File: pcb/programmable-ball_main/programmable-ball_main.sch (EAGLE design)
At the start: 19 parts, among them J1 12402012E212A, P1 S2B-ZR-SM4A-TF, Q1 DMG2305UX-13, SW1 CAS-120CAS-120B1, U1 MDBT50Q-1MV2, U2 AP2112K-3.3TRG1, Y1 FC-135_32.7680KA-A0

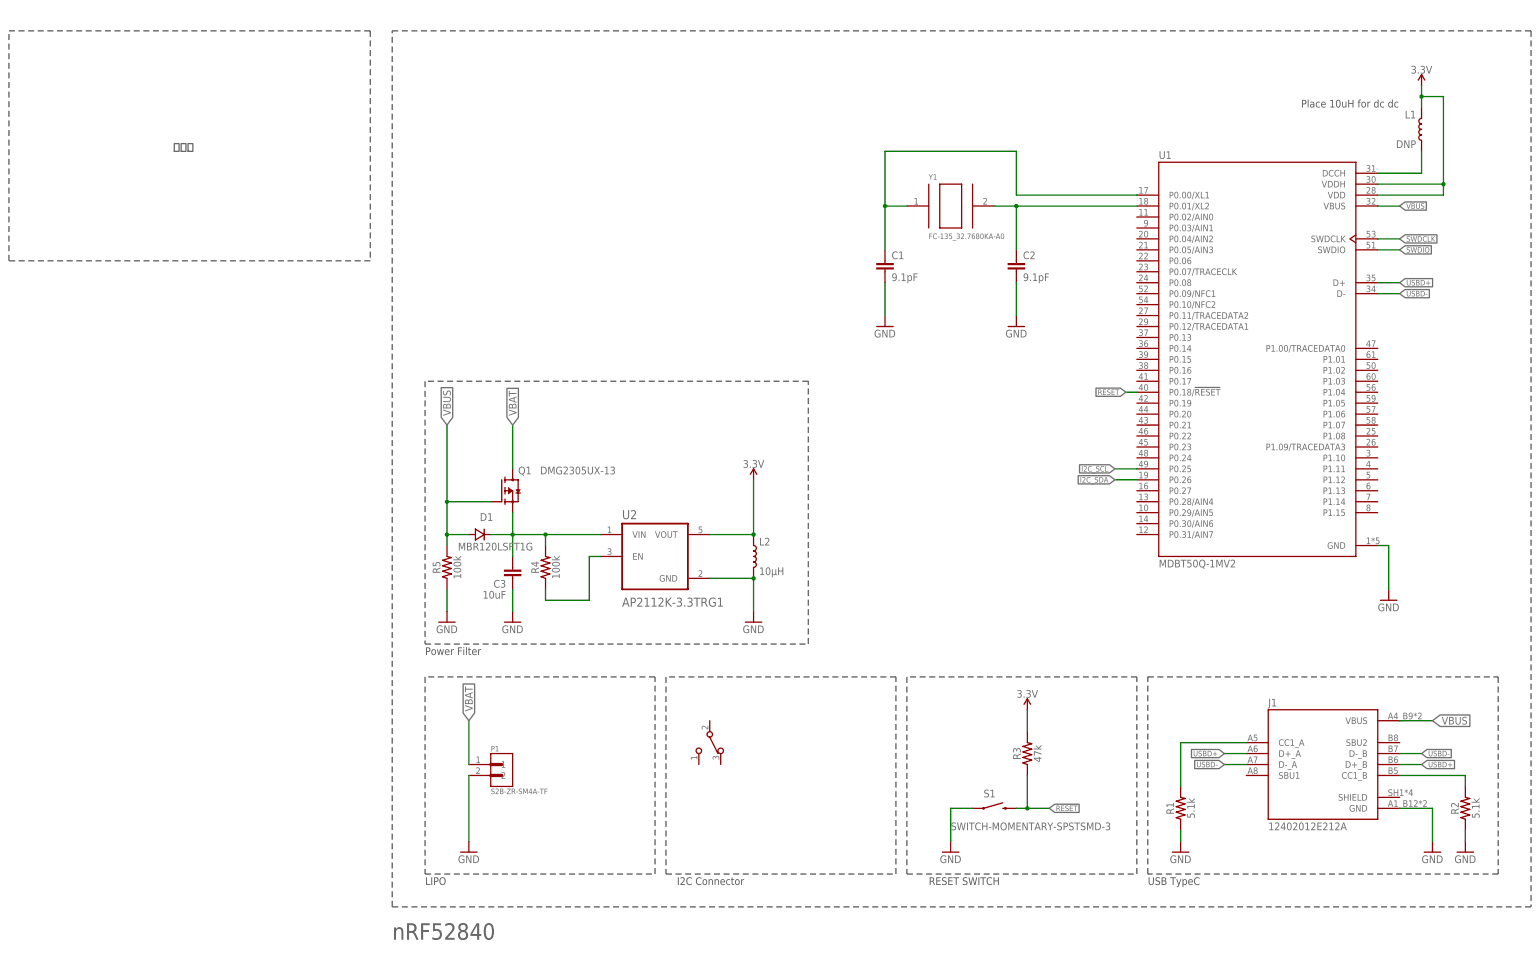
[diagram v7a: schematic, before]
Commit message: 主電源スイッチとリポ充放電素子を追加 #4
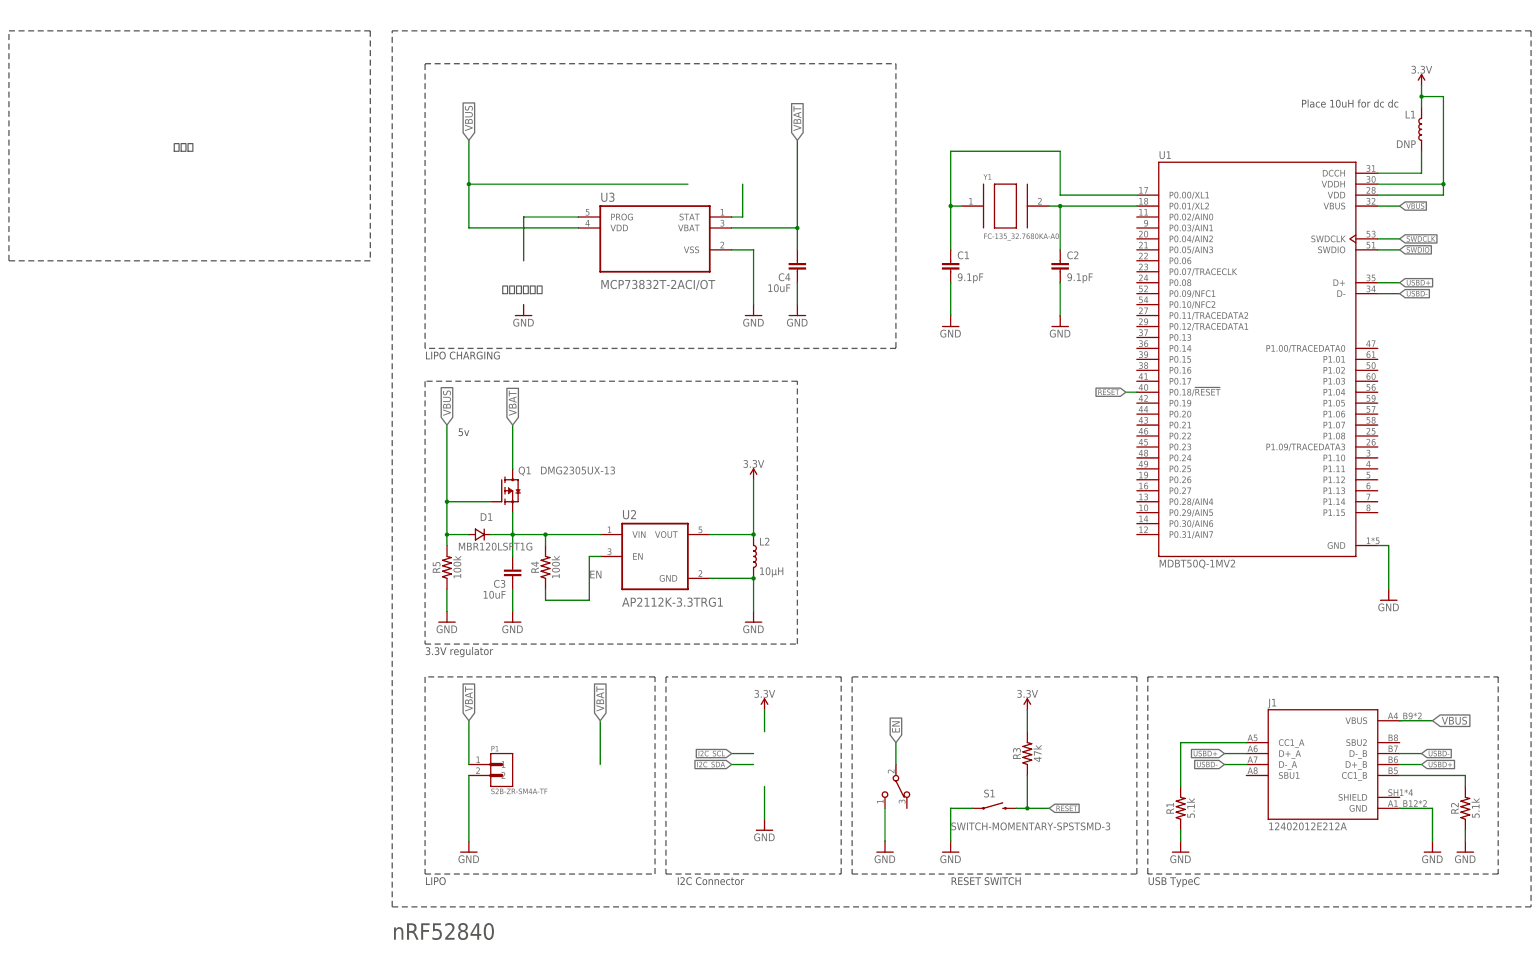
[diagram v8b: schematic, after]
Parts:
- added C4: 10uF, SparkFun-Capacitors:10UF-0402T-6.3V-20%
- added U3: MCP73832T-2ACI/OT, MCP73832T-2ACI_OT:MCP73832T-2ACI/OT
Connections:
- removed net I2C_SCL: U1.P0.25
- removed net I2C_SDA: U1.P0.26
- new net EN: R4.1, SW1.2, U2.EN
- new net N$8: U3.STAT
- net GND: now also C4.1, SW1.1, U3.VSS
- net N$7: now also U3.PROG; no longer R4.1, U2.EN
- net VBAT: now also C4.2, U3.VBAT
- net VBUS: now also U3.VDD
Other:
- note added: "3.3V regulator"
- note added: "5v"
- note added: "LIPO CHARGING"
- note added: "抵抗値調べて"
- note removed: "Power Filter"
- moved on the sheet: C1, C2, Y1
